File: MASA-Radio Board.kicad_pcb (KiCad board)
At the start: 4 copper layers, 75.8 x 76.2 mm, 73 parts, among them IC1 FAN4010IL6X_F113, IC2 FAN4010IL6X_F113, J1 Conn_01x02, J2 Conn_01x02_Male, J3 Conn_01x02_Male, J4 Conn_01x03_Male, J5 Conn_01x06, J6 SC_19-20, J7 Conn_01x06, J8 Conn_01x02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

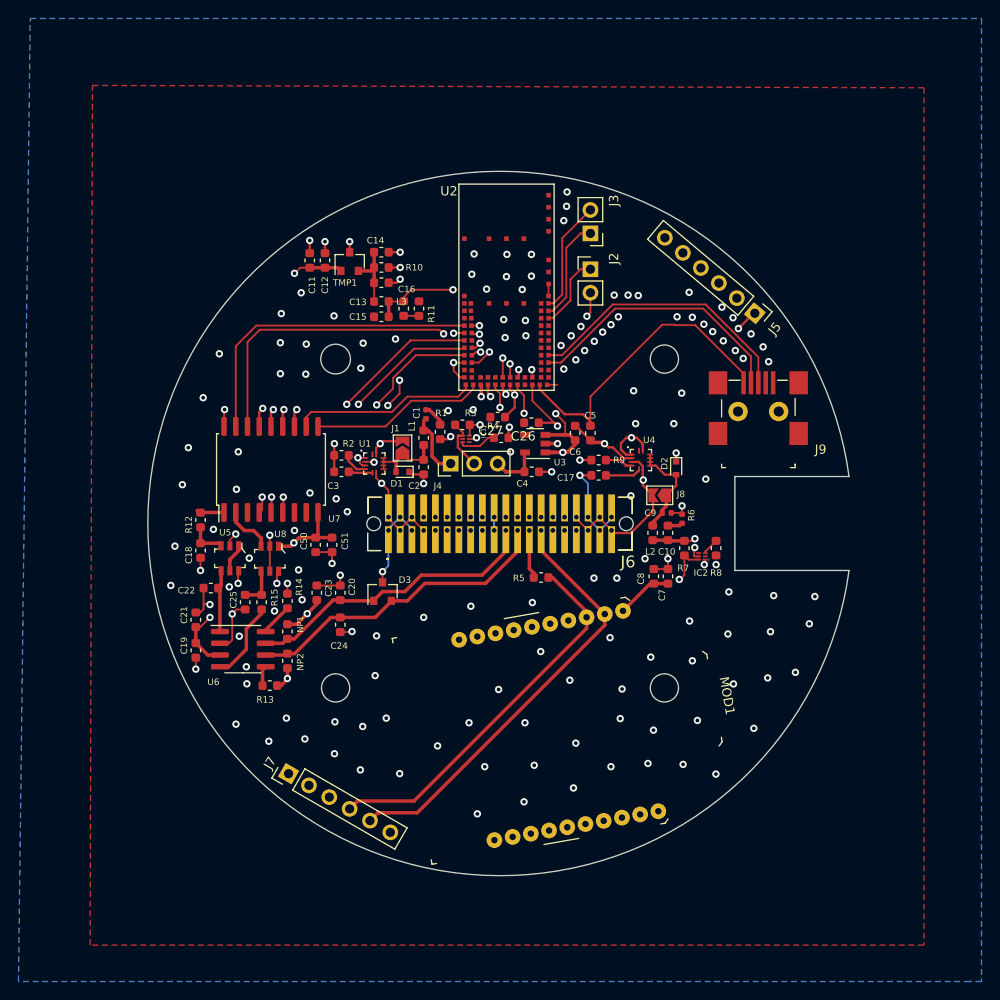
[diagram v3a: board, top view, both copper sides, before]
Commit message: Added filters and connected missing analog lines. Also fixed USB
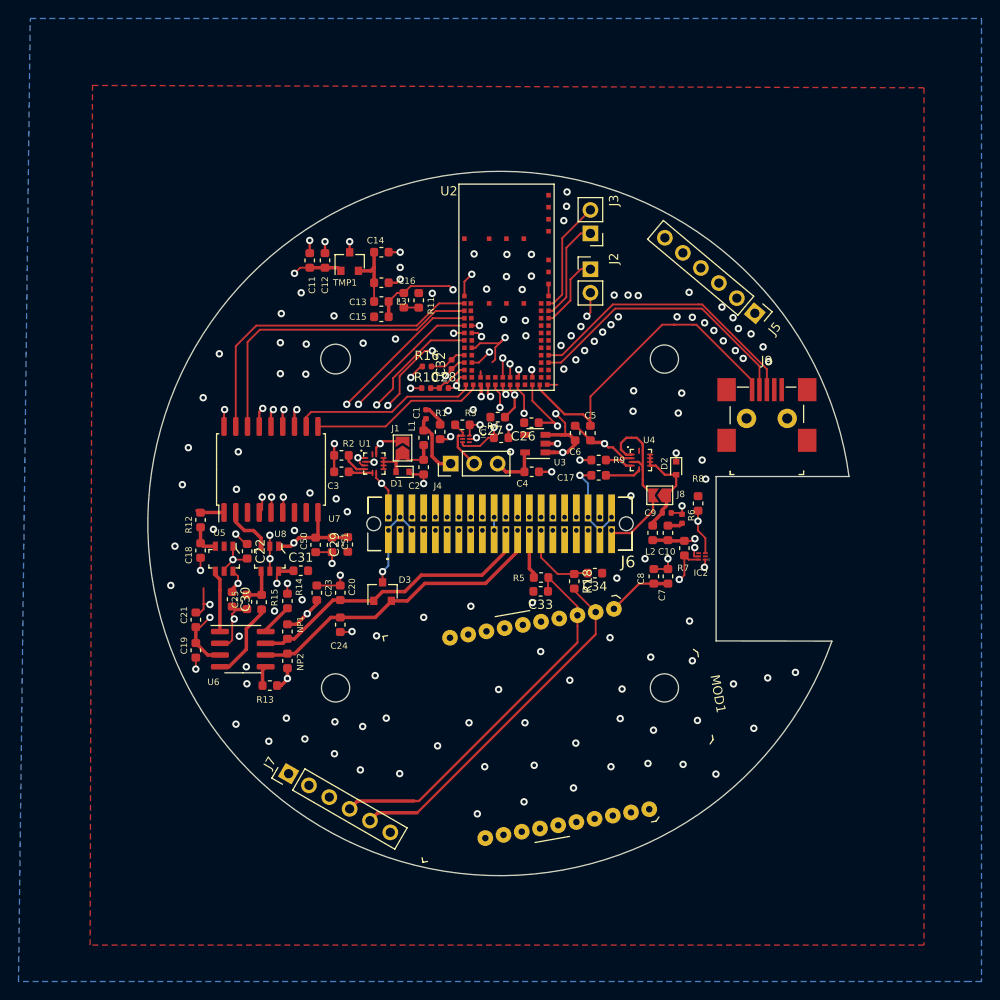
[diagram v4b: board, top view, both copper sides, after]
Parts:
- added C28: 1nF, Capacitor_SMD:C_0402_1005Metric, F.Cu at (146.3, 112.3)
- added C29: 10nF, Capacitor_SMD:C_0603_1608Metric, F.Cu at (135.9, 129.3)
- added C30: 10nF, Capacitor_SMD:C_0603_1608Metric, F.Cu at (123.4, 135.2)
- added C31: 10nF, Capacitor_SMD:C_0603_1608Metric, F.Cu at (130.9, 132.1)
- added C32: 1nF, Capacitor_SMD:C_0402_1005Metric, F.Cu at (147.2, 109.8)
- added C33: 2.2pF, Capacitor_SMD:C_0603_1608Metric, F.Cu at (156.8, 134.3)
- added C34: 470pF, Capacitor_SMD:C_0603_1608Metric, F.Cu at (162.7, 132.4)
- added R16: 1k, Resistor_SMD:R_0402_1005Metric, F.Cu at (144.5, 110.0)
- added R18: 470, Resistor_SMD:R_0603_1608Metric, F.Cu at (160.4, 133.2)
- C17: value 1uF -> 47nF
- C22: value 100pF -> 10nF
- C3: value 0.68uF -> 47nF
- R10: value 3.3k -> 1k; footprint Resistor_SMD:R_0603_1608Metric -> Resistor_SMD:R_0402_1005Metric
- moved R10 13.9 mm to (144.4, 112.4)
- moved C22 5.60 mm to (125.1, 130.0), turned to 270 degrees
- moved R8 5.21 mm to (173.8, 124.8), turned to 90 degrees
- moved J9 1.18 mm to (181.3, 120.4)
- moved MOD1 1.01 mm to (157.8, 148.6)
- moved C16 0.90 mm to (142.0, 102.9)
- moved R11 0.89 mm to (143.6, 102.9)
- moved U5 0.62 mm to (122.6, 130.8)
- moved C25 0.19 mm to (125.0, 135.5)
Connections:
- C22 pad 2: Net-(C22-Pad2) -> +3V3
- IC2 pad 3: Net-(IC2-Pad3) -> 5VSense
- J6 pad 27: XBee_TX -> Net-(C34-Pad2)
- R10 pad 1: Net-(C13-Pad1) -> 5VSense
- R10 pad 2: GND -> Net-(C28-Pad1)
- R8 pad 1: Net-(IC2-Pad3) -> 5VSense
- U2 pad 45: Net-(U2-Pad45) -> Net-(C28-Pad1)
- U2 pad 49: TX1RTS -> Net-(C32-Pad2)
- U2 pad 50: TX2RTS -> Net-(U2-Pad50)
- U2 pad 51: TX0RTS -> Net-(U2-Pad51)
- U2 pad 53: CAN_INT -> TX1RTS
- U2 pad 56: CS -> TX2RTS
- U2 pad 57: CAN_RST -> TX0RTS
- U2 pad 59: Net-(U2-Pad59) -> CAN_INT
- U2 pad 61: Net-(U2-Pad61) -> CS
- U2 pad 63: Net-(U2-Pad63) -> CAN_RST
- U5 pad 4: Net-(C22-Pad2) -> Net-(U5-Pad4)
- U6 pad 1: Net-(C22-Pad2) -> Net-(U5-Pad4)
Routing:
- net 5VSense: track 0.00 -> 50.9 mm, vias 0 -> 2
- net 3V3Sense: track 4.10 -> 18.5 mm, vias 0 -> 2
- net Net-(C34-Pad2): track 0.00 -> 10.9 mm
- net XBee_TX: track 47.3 -> 39.3 mm
- net Net-(C22-Pad2): track 6.87 -> 0.00 mm
- net Net-(U5-Pad4): track 0.00 -> 6.73 mm
- net +3V3: track 35.0 -> 39.6 mm, vias 5 -> 6
- net Net-(C28-Pad1): track 0.00 -> 4.46 mm
- net GND: track 105.2 -> 109.6 mm, vias 173 -> 165
- net Net-(C32-Pad2): track 0.00 -> 4.10 mm
- net 5V0: track 60.1 -> 56.7 mm, vias 3 -> 1
- net +5V: track 109.2 -> 112.2 mm, vias 6 -> 5
- net CS: track 36.5 -> 34.0 mm, vias 2 -> 0
- net Net-(IC2-Pad3): track 1.81 -> 0.00 mm
- net TX2RTS: track 32.3 -> 33.6 mm
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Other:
- outline, holes or cut-outs redrawn

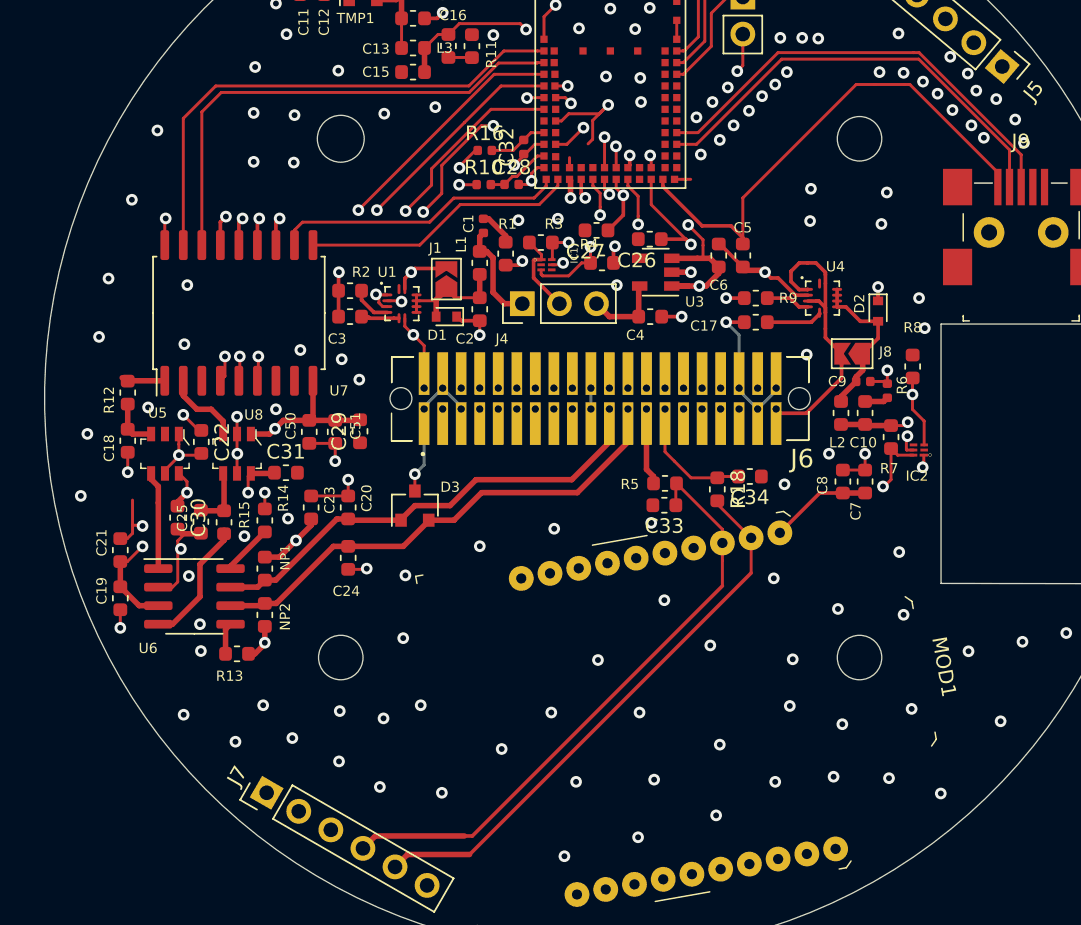
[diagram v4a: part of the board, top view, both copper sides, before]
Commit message: Added test points
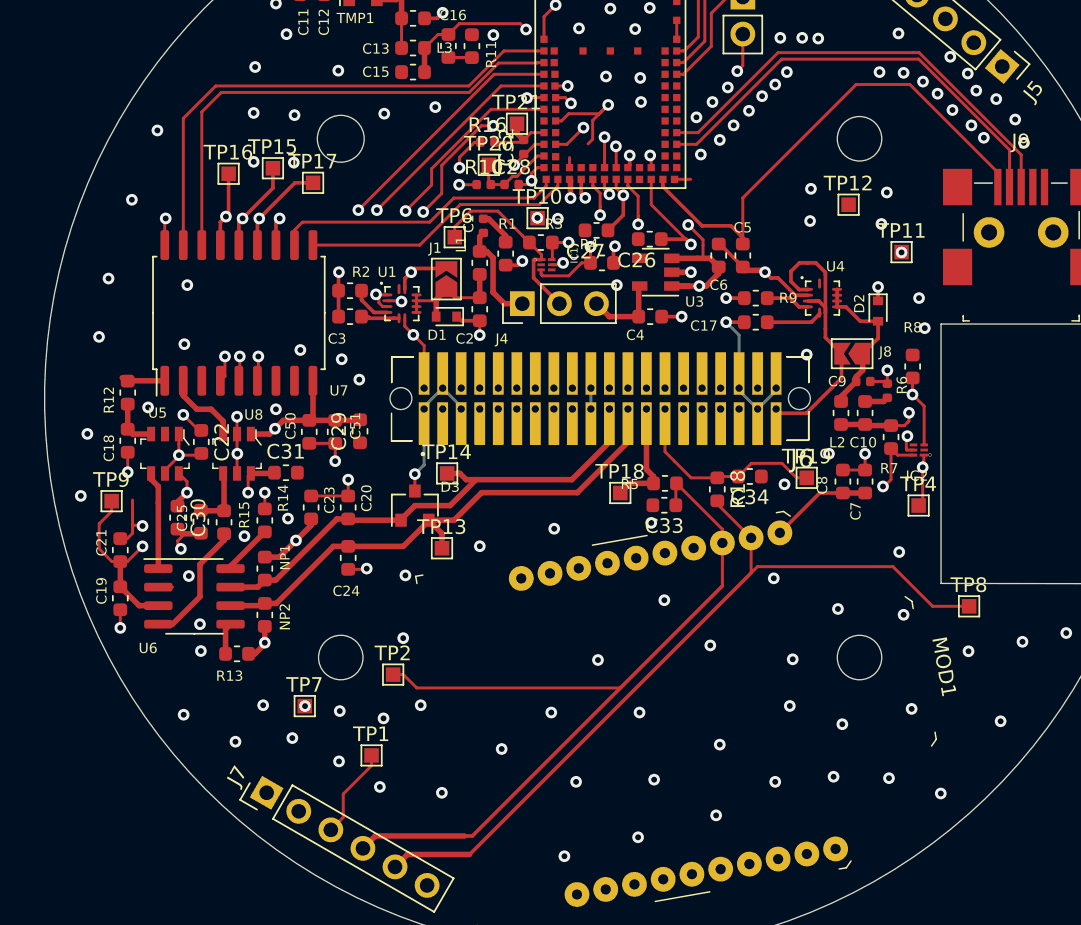
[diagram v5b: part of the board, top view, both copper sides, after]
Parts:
- added TP1: TestPoint, TestPoint:TestPoint_Pad_1.0x1.0mm, F.Cu at (136.7, 151.5)
- added TP10: TestPoint, TestPoint:TestPoint_Pad_1.0x1.0mm, F.Cu at (148.1, 114.7)
- added TP11: TestPoint, TestPoint:TestPoint_Pad_1.0x1.0mm, F.Cu at (173.1, 117.0)
- added TP12: TestPoint, TestPoint:TestPoint_Pad_1.0x1.0mm, F.Cu at (169.4, 113.7)
- added TP13: TestPoint, TestPoint:TestPoint_Pad_1.0x1.0mm, F.Cu at (141.6, 137.3)
- added TP14: TestPoint, TestPoint:TestPoint_Pad_1.0x1.0mm, F.Cu at (141.9, 132.2)
- added TP15: TestPoint, TestPoint:TestPoint_Pad_1.0x1.0mm, F.Cu at (130.0, 111.2)
- added TP16: TestPoint, TestPoint:TestPoint_Pad_1.0x1.0mm, F.Cu at (126.9, 111.6)
- added TP17: TestPoint, TestPoint:TestPoint_Pad_1.0x1.0mm, F.Cu at (132.7, 112.2)
- added TP18: TestPoint, TestPoint:TestPoint_Pad_1.0x1.0mm, F.Cu at (153.8, 133.5)
- added TP19: TestPoint, TestPoint:TestPoint_Pad_1.0x1.0mm, F.Cu at (166.6, 132.5)
- added TP2: TestPoint, TestPoint:TestPoint_Pad_1.0x1.0mm, F.Cu at (138.2, 145.9)
- added TP20: TestPoint, TestPoint:TestPoint_Pad_1.0x1.0mm, F.Cu at (144.8, 111.0)
- added TP21: TestPoint, TestPoint:TestPoint_Pad_1.0x1.0mm, F.Cu at (146.7, 108.2)
- added TP4: TestPoint, TestPoint:TestPoint_Pad_1.0x1.0mm, F.Cu at (174.2, 134.4)
- added TP6: TestPoint, TestPoint:TestPoint_Pad_1.0x1.0mm, F.Cu at (142.4, 116.0)
- added TP7: TestPoint, TestPoint:TestPoint_Pad_1.0x1.0mm, F.Cu at (132.2, 148.1)
- added TP8: TestPoint, TestPoint:TestPoint_Pad_1.0x1.0mm, F.Cu at (177.7, 141.3)
- added TP9: TestPoint, TestPoint:TestPoint_Pad_1.0x1.0mm, F.Cu at (118.9, 134.1)
- moved R16 0.59 mm to (144.7, 109.5)
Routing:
- net XBee_TX: track 39.3 -> 55.5 mm
- net XBee_RX: track 41.9 -> 57.9 mm
- net Net-(IC1-Pad1): track 5.78 -> 12.9 mm
- net V_IN_5V0: track 112.2 -> 118.5 mm
- net Net-(C34-Pad2): track 10.9 -> 16.4 mm
- net +5V: track 112.2 -> 117.7 mm
- net SPI_CLK: track 30.0 -> 34.7 mm
- net SPI_MOSI: track 31.1 -> 35.4 mm
- net Net-(C10-Pad1): track 8.49 -> 12.5 mm
- net SPI_MISO: track 32.4 -> 35.5 mm
- net GND: track 109.6 -> 106.9 mm, vias 165 -> 164
- net Net-(J6-Pad25): track 5.30 -> 7.85 mm
- net 5VSense: track 50.9 -> 53.2 mm, vias 2 -> 3
- net CAN_L: track 34.2 -> 36.5 mm
- net CAN_H: track 32.5 -> 34.6 mm
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
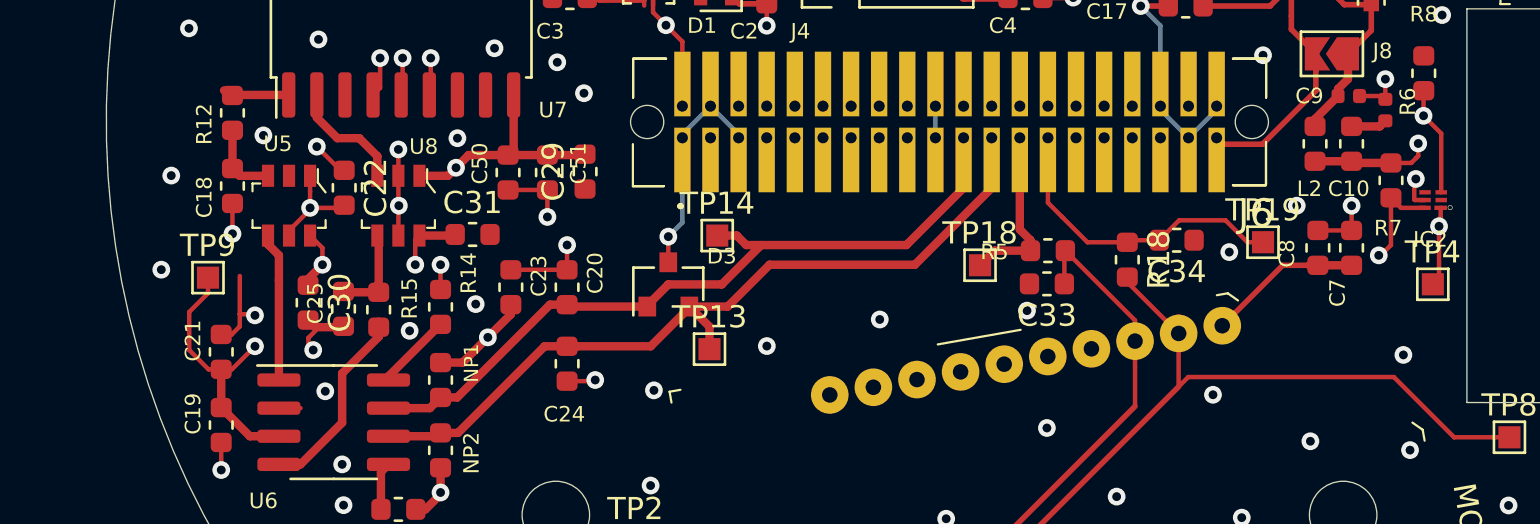
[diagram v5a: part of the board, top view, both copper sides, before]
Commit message: Added 0 Ohm resistors
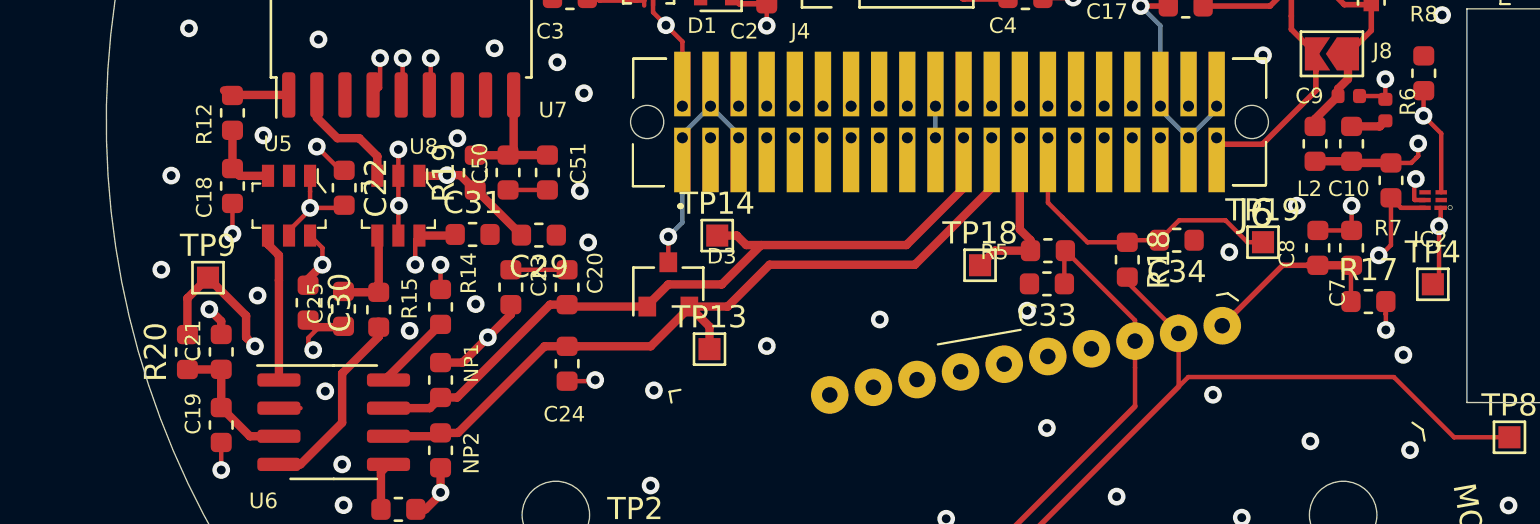
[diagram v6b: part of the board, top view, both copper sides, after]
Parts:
- added R17: 0, Resistor_SMD:R_0603_1608Metric, F.Cu at (171.3, 135.1)
- added R19: 0, Resistor_SMD:R_0603_1608Metric, F.Cu at (131.0, 129.3)
- added R20: 0, Resistor_SMD:R_0603_1608Metric, F.Cu at (118.0, 137.4)
- moved C29 3.55 mm to (133.9, 132.1), turned to 180 degrees
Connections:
- C19 pad 2: +5V -> Net-(C19-Pad2)
- C21 pad 1: +5V -> Net-(C19-Pad2)
- C50 pad 1: +3V3 -> Net-(C50-Pad1)
- C51 pad 2: +3V3 -> Net-(C50-Pad1)
- C7 pad 2: +3V3 -> Net-(C7-Pad2)
- C8 pad 2: +3V3 -> Net-(C7-Pad2)
- MOD1 pad 1: +3V3 -> Net-(C7-Pad2)
- U6 pad 3: +5V -> Net-(C19-Pad2)
- U7 pad 9: +3V3 -> Net-(C50-Pad1)
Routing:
- net +3V3: track 39.6 -> 29.2 mm, vias 7 -> 8
- net Net-(C7-Pad2): track 0.00 -> 9.01 mm
- net Net-(C19-Pad2): track 0.00 -> 6.40 mm
- net Net-(C50-Pad1): track 0.00 -> 6.08 mm
- net +5V: track 117.7 -> 112.3 mm
- net GND: track 106.9 -> 101.9 mm, vias 164 -> 165

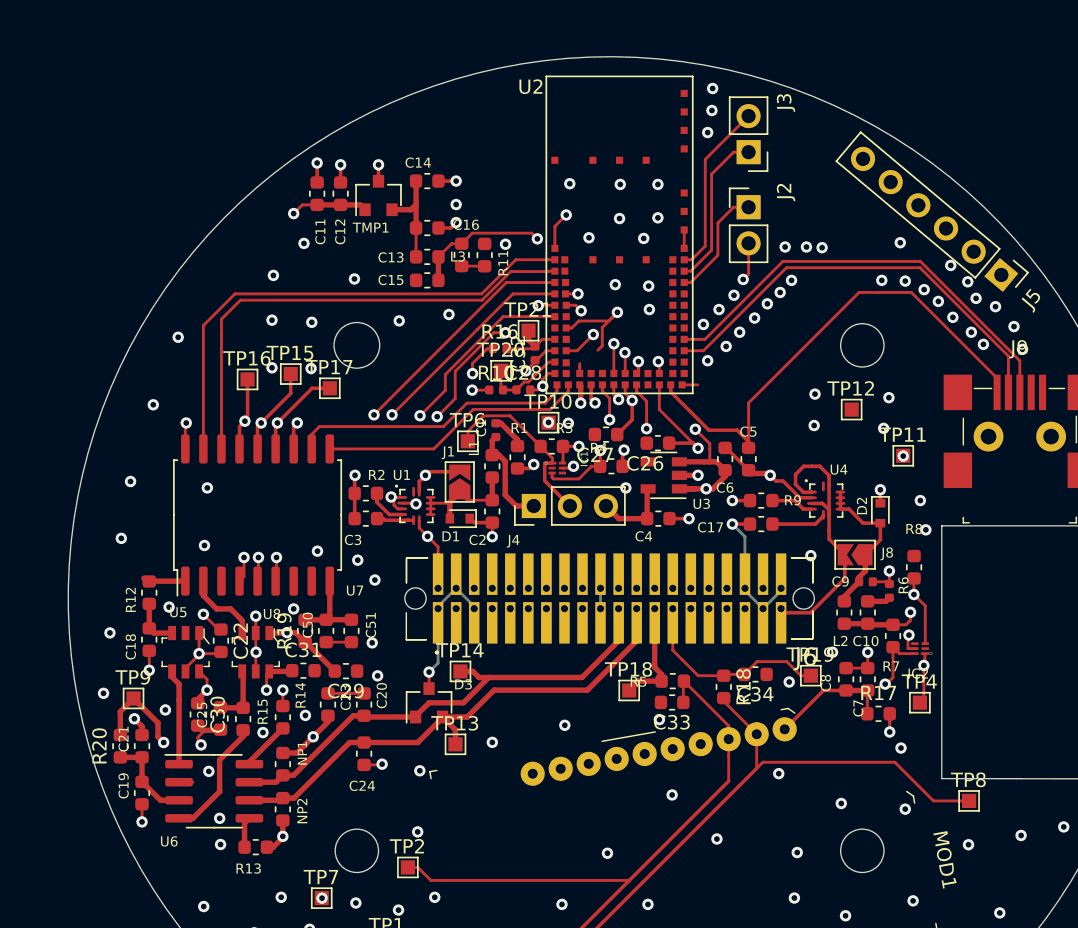
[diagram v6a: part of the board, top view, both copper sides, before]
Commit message: Updated silk screen
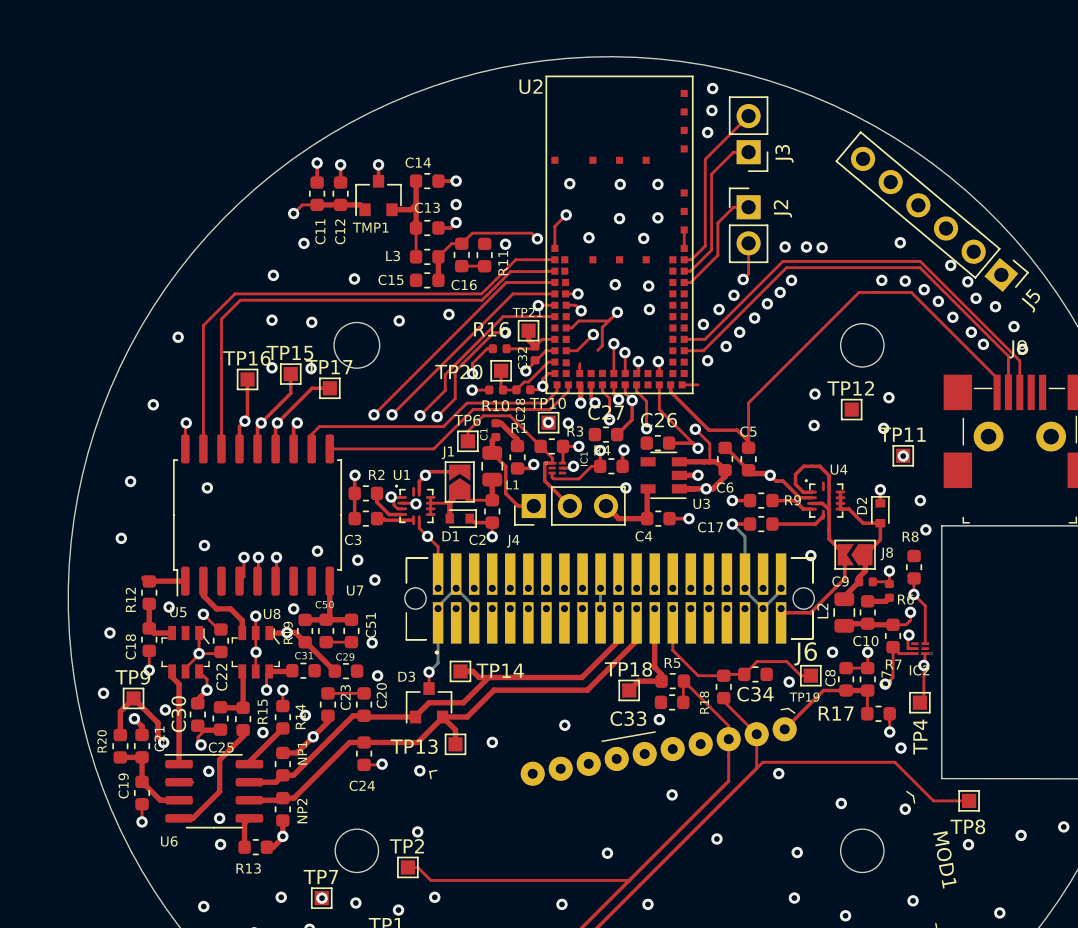
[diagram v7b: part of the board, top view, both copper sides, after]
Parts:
- L1, L2: footprint Inductor_SMD:L_0603_1608Metric -> Inductor_SMD:L_0805_2012Metric
